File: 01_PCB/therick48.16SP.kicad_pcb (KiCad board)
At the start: 2 copper layers, 308.9 x 75.8 mm, 181 parts, among them J1 TYPE-C-31-M12_13, J2 AVR-ISP-6_mod, K1 KEYSW, K10 KEYSW, K11 KEYSW, K12 KEYSW, K13 KEYSW, K14 KEYSW, K15 KEYSW, K16 KEYSW, K17 KEYSW, K18 KEYSW, K19 KEYSW, K2 KEYSW, K20 KEYSW, K21 KEYSW, K22 KEYSW, K23 KEYSW, K24 KEYSW, K25 KEYSW, K26 KEYSW, K27 KEYSW, K28 KEYSW, K29 KEYSW, K3 KEYSW, K30 KEYSW, K31 KEYSW, K32 KEYSW, K33 KEYSW, K34 KEYSW, K35 KEYSW, K36 KEYSW, K37 KEYSW, K38 KEYSW, K39 KEYSW, K4 KEYSW, K40 KEYSW, K41 KEYSW, K42 KEYSW, K43 KEYSW, K44 KEYSW, K45 KEYSW, K46 KEYSW, K47 KEYSW, K48 KEYSW, K49 KEYSW, K5 KEYSW, K50 KEYSW, K51 KEYSW, K52 KEYSW, K53 KEYSW, K54 KEYSW, K55 KEYSW, K56 KEYSW, K57 KEYSW, K58 KEYSW, K59 KEYSW, K6 KEYSW, K60 KEYSW, K61 KEYSW, K62 KEYSW, K63 KEYSW, K64 KEYSW, K7 KEYSW, K8 KEYSW, K9 KEYSW, SW1 SW_PUSH, SW2 Rotary_Encoder_Switch, U1 ATMEGA32U4, U10 HOLE, U11 HOLE, U2 HOLE, U3 USBLC6-2SC6, U4 HOLE, U5 HOLE, U6 HOLE, U7 HOLE, U8 HOLE, U9 HOLE, Y1 16MHz

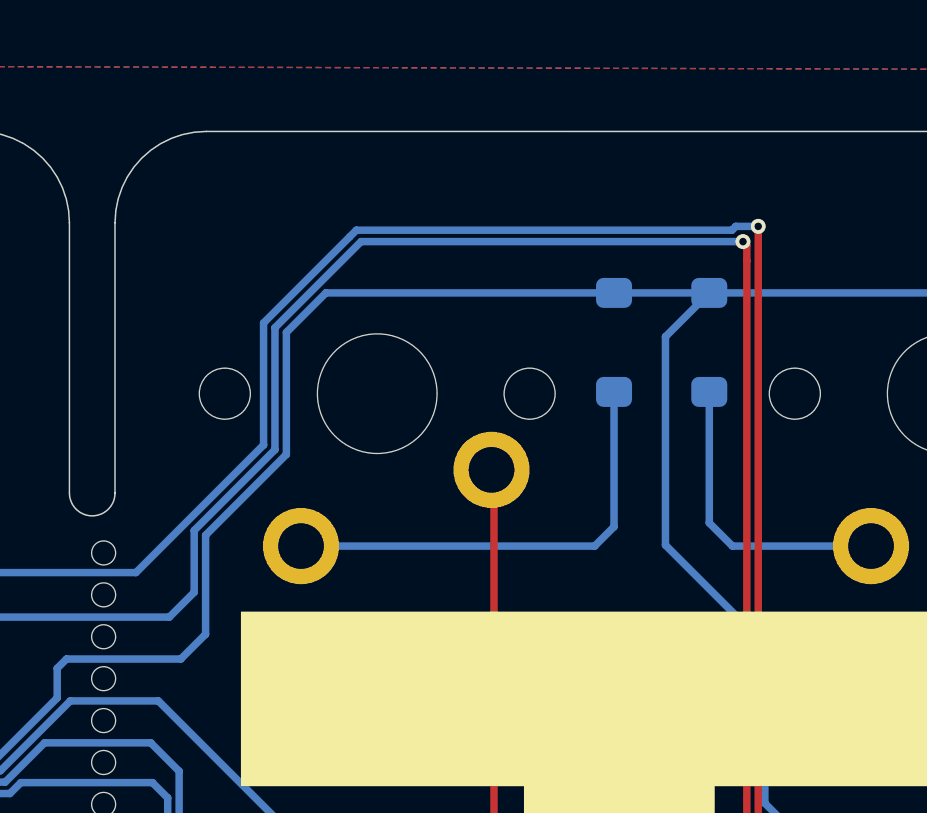
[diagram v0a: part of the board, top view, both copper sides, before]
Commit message: Added encoder
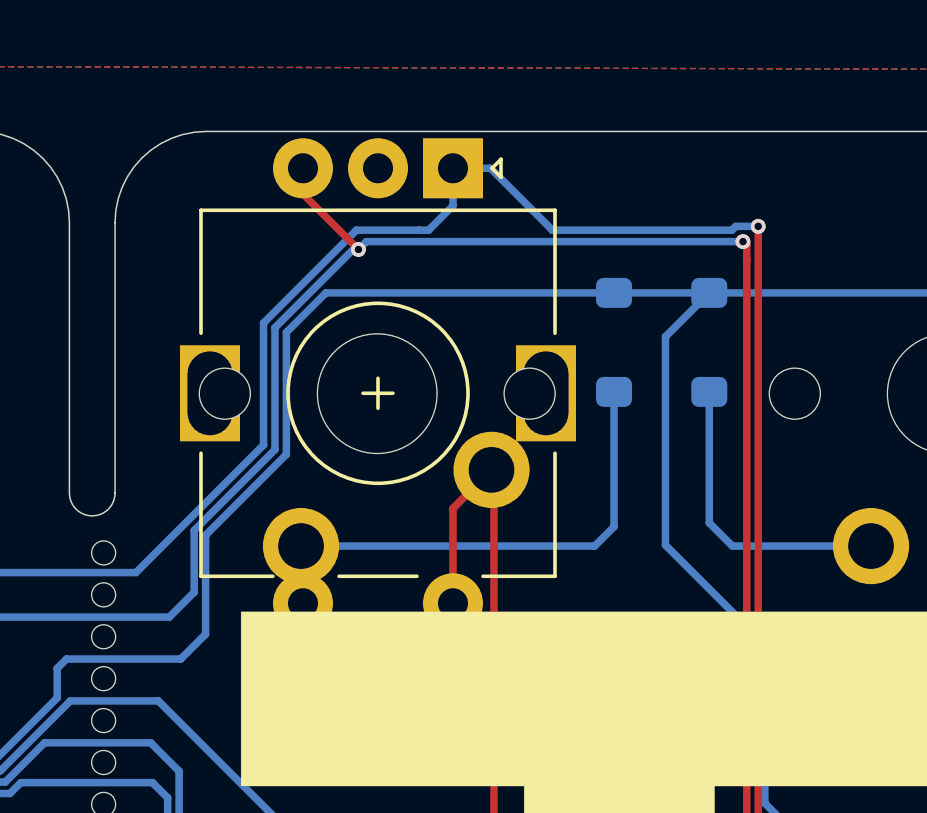
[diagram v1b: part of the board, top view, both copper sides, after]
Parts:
- added SW3: Rotary_Encoder_Switch, Keebio-Parts:RotaryEncoder_EC11, F.Cu at (144.8, 52.4)
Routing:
- net col0: track 77.6 -> 82.6 mm
- net EncB: track 122.6 -> 126.1 mm, vias 2 -> 3
- net EncA: track 115.8 -> 118.2 mm
- net Net-(D1-Pad2): track 15.2 -> 17.1 mm
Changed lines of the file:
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@@
     (thickness 1.6)
     (drawings 132)
-    (tracks 1040)
+    (tracks 1056)
     (zones 0)
-    (modules 181)
+    (modules 182)
     (nets 104)
   )
@@
     (uvia_drill 0.2)
   )
+  (module Keebio-Parts:RotaryEncoder_EC11 (layer F.Cu)
+    (at 144.805399 52.427302 270)
+    (descr "Alps rotary encoder, EC12E... with switch, vertical shaft, http://www.alps.com/prod/info/E/HTML/Encoder/Incremental/EC11/EC11E15204A3.html")
+    (tags "rotary encoder")
+    (fp_text reference SW3 (at -4.7 -7.2 90) (layer F.Fab)
+      (effects (font (size 1 1) (thickness 0.15)))
+    )
+    (fp_text value Rotary_Encoder_Switch (at 0 7.9 90) (layer F.Fab)
+      (effects (font (size 1 1) (thickness 0.15)))
+    )
+    (fp_circle (center 0 0) (end 3 0) (layer F.Fab) (width 0.12))
+    (fp_circle (center 0 0) (end 3 0) (layer F.SilkS) (width 0.12))
+    (fp_line (start 8.5 7.1) (end -9 7.1) (layer F.CrtYd) (width 0.05))
+    (fp_line (start 8.5 7.1) (end 8.5 -7.1) (layer F.CrtYd) (width 0.05))
+    (fp_line (start -9 -7.1) (end -9 7.1) (layer F.CrtYd) (width 0.05))
+    (fp_line (start -9 -7.1) (end 8.5 -7.1) (layer F.CrtYd) (width 0.05))
+    (fp_line (start -5 -5.8) (end 6 -5.8) (layer F.Fab) (width 0.12))
+    (fp_line (start 6 -5.8) (end 6 5.8) (layer F.Fab) (width 0.12))
+    (fp_line (start 6 5.8) (end -6 5.8) (layer F.Fab) (width 0.12))
+    (fp_line (start -6 5.8) (end -6 -4.7) (layer F.Fab) (width 0.12))
+    (fp_line (start -6 -4.7) (end -5 -5.8) (layer F.Fab) (width 0.12))
+    (fp_line (start 2 -5.9) (end 6.1 -5.9) (layer F.SilkS) (width 0.12))
+    (fp_line (start 6.1 5.9) (end 2 5.9) (layer F.SilkS) (width 0.12))
+    (fp_line (start -2 5.9) (end -6.1 5.9) (layer F.SilkS) (width 0.12))
+    (fp_line (start -2 -5.9) (end -6.1 -5.9) (layer F.SilkS) (width 0.12))
+    (fp_line (start -6.1 -5.9) (end -6.1 5.9) (layer F.SilkS) (width 0.12))
+    (fp_line (start -7.5 -3.8) (end -7.8 -4.1) (layer F.SilkS) (width 0.12))
+    (fp_line (start -7.8 -4.1) (end -7.2 -4.1) (layer F.SilkS) (width 0.12))
+    (fp_line (start -7.2 -4.1) (end -7.5 -3.8) (layer F.SilkS) (width 0.12))
+    (fp_line (start 0 -3) (end 0 3) (layer F.Fab) (width 0.12))
+    (fp_line (start -3 0) (end 3 0) (layer F.Fab) (width 0.12))
+    (fp_line (start 6.1 -5.9) (end 6.1 -3.5) (layer F.SilkS) (width 0.12))
+    (fp_line (start 6.1 -1.3) (end 6.1 1.3) (layer F.SilkS) (width 0.12))
+    (fp_line (start 6.1 3.5) (end 6.1 5.9) (layer F.SilkS) (width 0.12))
+    (fp_line (start 0 -0.5) (end 0 0.5) (layer F.SilkS) (width 0.12))
+    (fp_line (start -0.5 0) (end 0.5 0) (layer F.SilkS) (width 0.12))
+    (fp_text user %R (at 3.6 3.8 90) (layer F.Fab)
+      (effects (font (size 1 1) (thickness 0.15)))
+    )
+    (pad A thru_hole rect (at -7.5 -2.5 270) (size 2 2) (drill 1) (layers *.Cu *.Mask)
+      (net 102 EncA))
+    (pad C thru_hole circle (at -7.5 0 270) (size 2 2) (drill 1) (layers *.Cu *.Mask)
+      (net 100 GND))
+    (pad B thru_hole circle (at -7.5 2.5 270) (size 2 2) (drill 1) (layers *.Cu *.Mask)
+      (net 103 EncB))
+    (pad MP thru_hole rect (at 0 -5.6 270) (size 3.2 2) (drill oval 2.8 1.5) (layers *.Cu *.Mask))
+    (pad MP thru_hole rect (at 0 5.6 270) (size 3.2 2) (drill oval 2.8 1.5) (layers *.Cu *.Mask))
+    (pad S2 thru_hole circle (at 7 -2.5 270) (size 2 2) (drill 1) (layers *.Cu *.Mask)
+      (net 60 col0))
+    (pad S1 thru_hole circle (at 7 2.5 270) (size 2 2) (drill 1) (layers *.Cu *.Mask)
+      (net 1 "Net-(D1-Pad2)"))
+    (model ${KISYS3DMOD}/Rotary_Encoder.3dshapes/RotaryEncoder_Alps_EC11E-Switch_Vertical_H20mm.wrl
+      (at (xyz 0 0 0))
+      (scale (xyz 1 1 1))
+      (rotate (xyz 0 0 0))
+    )
+  )
   (module Keeb_footprints:PIN_HEADER_1x6_OFFSET (layer B.Cu)
     (at 249.1032 61.69 180)
@@
   (segment (start 152.672999 56.875002) (end 152.027999 57.520002) (width 0.25) (layer B.Cu) (net 1))
   (segment (start 152.672999 52.381377) (end 152.672999 56.875002) (width 0.25) (layer B.Cu) (net 1))
+  (segment (start 142.305399 57.585402) (end 142.239999 57.520002) (width 0.25) (layer B.Cu) (net 1))
+  (segment (start 142.305399 59.427302) (end 142.305399 57.585402) (width 0.25) (layer B.Cu) (net 1))
   (segment (start 156.619999 57.520002) (end 161.239999 57.520002) (width 0.25) (layer B.Cu) (net 2))
   (segment (start 155.847999 56.748002) (end 156.619999 57.520002) (width 0.25) (layer B.Cu) (net 2))
@@
   (segment (start 160.595787 83.305002) (end 158.577787 85.323002) (width 0.25) (layer B.Cu) (net 60))
   (segment (start 148.672499 54.970002) (end 148.672499 87.204499) (width 0.25) (layer F.Cu) (net 60))
+  (segment (start 147.305399 56.264602) (end 148.589999 54.980002) (width 0.25) (layer F.Cu) (net 60))
+  (segment (start 147.305399 59.427302) (end 147.305399 56.264602) (width 0.25) (layer F.Cu) (net 60))
   (segment (start 169.437499 88.405002) (end 168.077999 88.405002) (width 0.25) (layer B.Cu) (net 61))
   (segment (start 167.589999 88.893002) (end 167.589999 92.980002) (width 0.25) (layer B.Cu) (net 61))
@@
   (segment (start 157.48 46.863) (end 156.732598 46.863) (width 0.25) (layer B.Cu) (net 102))
   (segment (start 143.860577 47.213596) (end 140.990979 50.083192) (width 0.25) (layer B.Cu) (net 102))
-  (segment (start 156.604608 46.99099) (end 144.083182 46.99099) (width 0.25) (layer B.Cu) (net 102))
+  (segment (start 148.555399 44.927302) (end 147.305399 44.927302) (width 0.25) (layer B.Cu) (net 102))
+  (segment (start 150.60849 46.980393) (end 148.555399 44.927302) (width 0.25) (layer B.Cu) (net 102))
+  (segment (start 150.60849 46.99099) (end 150.60849 46.980393) (width 0.25) (layer B.Cu) (net 102))
+  (segment (start 156.604608 46.99099) (end 150.60849 46.99099) (width 0.25) (layer B.Cu) (net 102))
+  (segment (start 146.491711 46.99099) (end 146.170729 46.99099) (width 0.25) (layer B.Cu) (net 102))
+  (segment (start 147.305399 46.177302) (end 146.491711 46.99099) (width 0.25) (layer B.Cu) (net 102))
+  (segment (start 147.305399 44.927302) (end 147.305399 46.177302) (width 0.25) (layer B.Cu) (net 102))
+  (segment (start 146.170729 46.99099) (end 144.083182 46.99099) (width 0.25) (layer B.Cu) (net 102))
   (segment (start 171.037499 89.405002) (end 170.617509 89.824992) (width 0.25) (layer B.Cu) (net 103))
   (segment (start 171.037499 88.405002) (end 171.037499 89.405002) (width 0.25) (layer B.Cu) (net 103))
@@
   (segment (start 157.09999 47.49899) (end 156.972 47.371) (width 0.25) (layer F.Cu) (net 103))
   (segment (start 157.09999 48.00699) (end 157.09999 47.49899) (width 0.25) (layer F.Cu) (net 103))
-  (segment (start 125.603 46.863) (end 118.780924 46.863) (width 0.25) (layer B.Cu) (net 103))
-  (segment (start 141.370989 54.307598) (end 138.678839 56.999746) (width 0.25) (layer B.Cu) (net 103))
+  (segment (start 144.417351 47.371) (end 144.154048 47.634303) (width 0.25) (layer B.Cu) (net 103))
+  (via (at 144.154048 47.634303) (size 0.5) (drill 0.25) (layers F.Cu B.Cu) (net 103))
+  (segment (start 156.972 47.371) (end 144.417351 47.371) (width 0.25) (layer B.Cu) (net 103))
+  (segment (start 142.305399 45.785654) (end 142.305399 44.927302) (width 0.25) (layer F.Cu) (net 103))
+  (segment (start 144.154048 47.634303) (end 142.305399 45.785654) (width 0.25) (layer F.Cu) (net 103))
   (segment (start 127.635 56.036415) (end 127.635 48.895) (width 0.25) (layer B.Cu) (net 103))
-  (segment (start 127.635 48.895) (end 125.603 46.863) (width 0.25) (layer B.Cu) (net 103))
-  (segment (start 138.678839 56.999746) (end 138.678839 59.060161) (width 0.25) (layer B.Cu) (net 103))
   (segment (start 131.486421 59.887836) (end 127.635 56.036415) (width 0.25) (layer B.Cu) (net 103))
+  (segment (start 141.370989 50.240597) (end 141.370989 54.307598) (width 0.25) (layer B.Cu) (net 103))
+  (segment (start 138.678839 56.999746) (end 138.678839 59.060161) (width 0.25) (layer B.Cu) (net 103))
+  (segment (start 137.851164 59.887836) (end 131.486421 59.887836) (width 0.25) (layer B.Cu) (net 103))
+  (segment (start 141.370989 54.307598) (end 138.678839 56.999746) (width 0.25) (layer B.Cu) (net 103))
+  (segment (start 144.154048 47.634303) (end 143.977284 47.634303) (width 0.25) (layer B.Cu) (net 103))
+  (segment (start 143.977284 47.634303) (end 141.370989 50.240597) (width 0.25) (layer B.Cu) (net 103))
   (segment (start 118.780924 46.863) (end 116.845086 44.927162) (width 0.25) (layer B.Cu) (net 103))
+  (segment (start 125.603 46.863) (end 118.780924 46.863) (width 0.25) (layer B.Cu) (net 103))
+  (segment (start 127.635 48.895) (end 125.603 46.863) (width 0.25) (layer B.Cu) (net 103))
   (segment (start 138.678839 59.060161) (end 137.851164 59.887836) (width 0.25) (layer B.Cu) (net 103))
-  (segment (start 156.972 47.371) (end 144.240587 47.371) (width 0.25) (layer B.Cu) (net 103))
-  (segment (start 137.851164 59.887836) (end 131.486421 59.887836) (width 0.25) (layer B.Cu) (net 103))
-  (segment (start 141.370989 50.240597) (end 141.370989 54.307598) (width 0.25) (layer B.Cu) (net 103))
-  (segment (start 144.240587 47.371) (end 141.370989 50.240597) (width 0.25) (layer B.Cu) (net 103))
   (zone (net 100) (net_name GND) (layer F.Cu) (hatch edge 0.508)
     (connect_pads (clearance 0.25))

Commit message: Update
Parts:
- removed U8: HOLE, Artwork:THERICK
- added SW4: Rotary_Encoder_Switch, Keebio-Parts:RotaryEncoder_EC11, F.Cu at (119.3, 109.4)
- added SW5: Rotary_Encoder_Switch, Keebio-Parts:RotaryEncoder_EC11, F.Cu at (144.8, 109.4)
- added SW6: Rotary_Encoder_Switch, Keebio-Parts:RotaryEncoder_EC11, F.Cu at (353.8, 109.4)
- added SW7: Rotary_Encoder_Switch, Keebio-Parts:RotaryEncoder_EC11, F.Cu at (353.8, 52.4)
- added SW8: Rotary_Encoder_Switch, Keebio-Parts:RotaryEncoder_EC11, F.Cu at (239.8, 109.4)
- added SW9: Rotary_Encoder_Switch, Keebio-Parts:RotaryEncoder_EC11, F.Cu at (258.8, 109.4)
- moved U9 43.9 mm to (268.2, 59.6)
- moved D64 2.67 mm to (114.0, 103.1)
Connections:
- U1 pad 18: (no net) -> EncD
- U1 pad 19: (no net) -> EncC
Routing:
- net EncD: track 0.00 -> 278.7 mm, vias 0 -> 2
- net EncC: track 0.00 -> 276.5 mm, vias 0 -> 2
- net EncB: track 126.1 -> 358.1 mm, vias 3 -> 6
- net EncA: track 118.2 -> 342.5 mm, vias 2 -> 4
- net VCC: track 217.5 -> 233.2 mm
- net col11: track 385.0 -> 395.0 mm
- net row0: track 351.1 -> 358.1 mm
- net col6: track 151.2 -> 156.2 mm
- net col5: track 135.4 -> 140.3 mm
- net col15: track 131.9 -> 136.8 mm
- net GND: track 23.0 -> 27.4 mm, vias 2 -> 3
- net Net-(D64-Pad2): track 9.49 -> 13.6 mm
- net Net-(D37-Pad2): track 22.8 -> 24.8 mm
- net Net-(D12-Pad2): track 10.7 -> 12.6 mm
- net Net-(D48-Pad2): track 10.3 -> 12.3 mm
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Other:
- board text added: "Encoder A"
- board text added: "Encoder B"
